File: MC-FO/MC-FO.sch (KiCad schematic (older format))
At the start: 0 parts

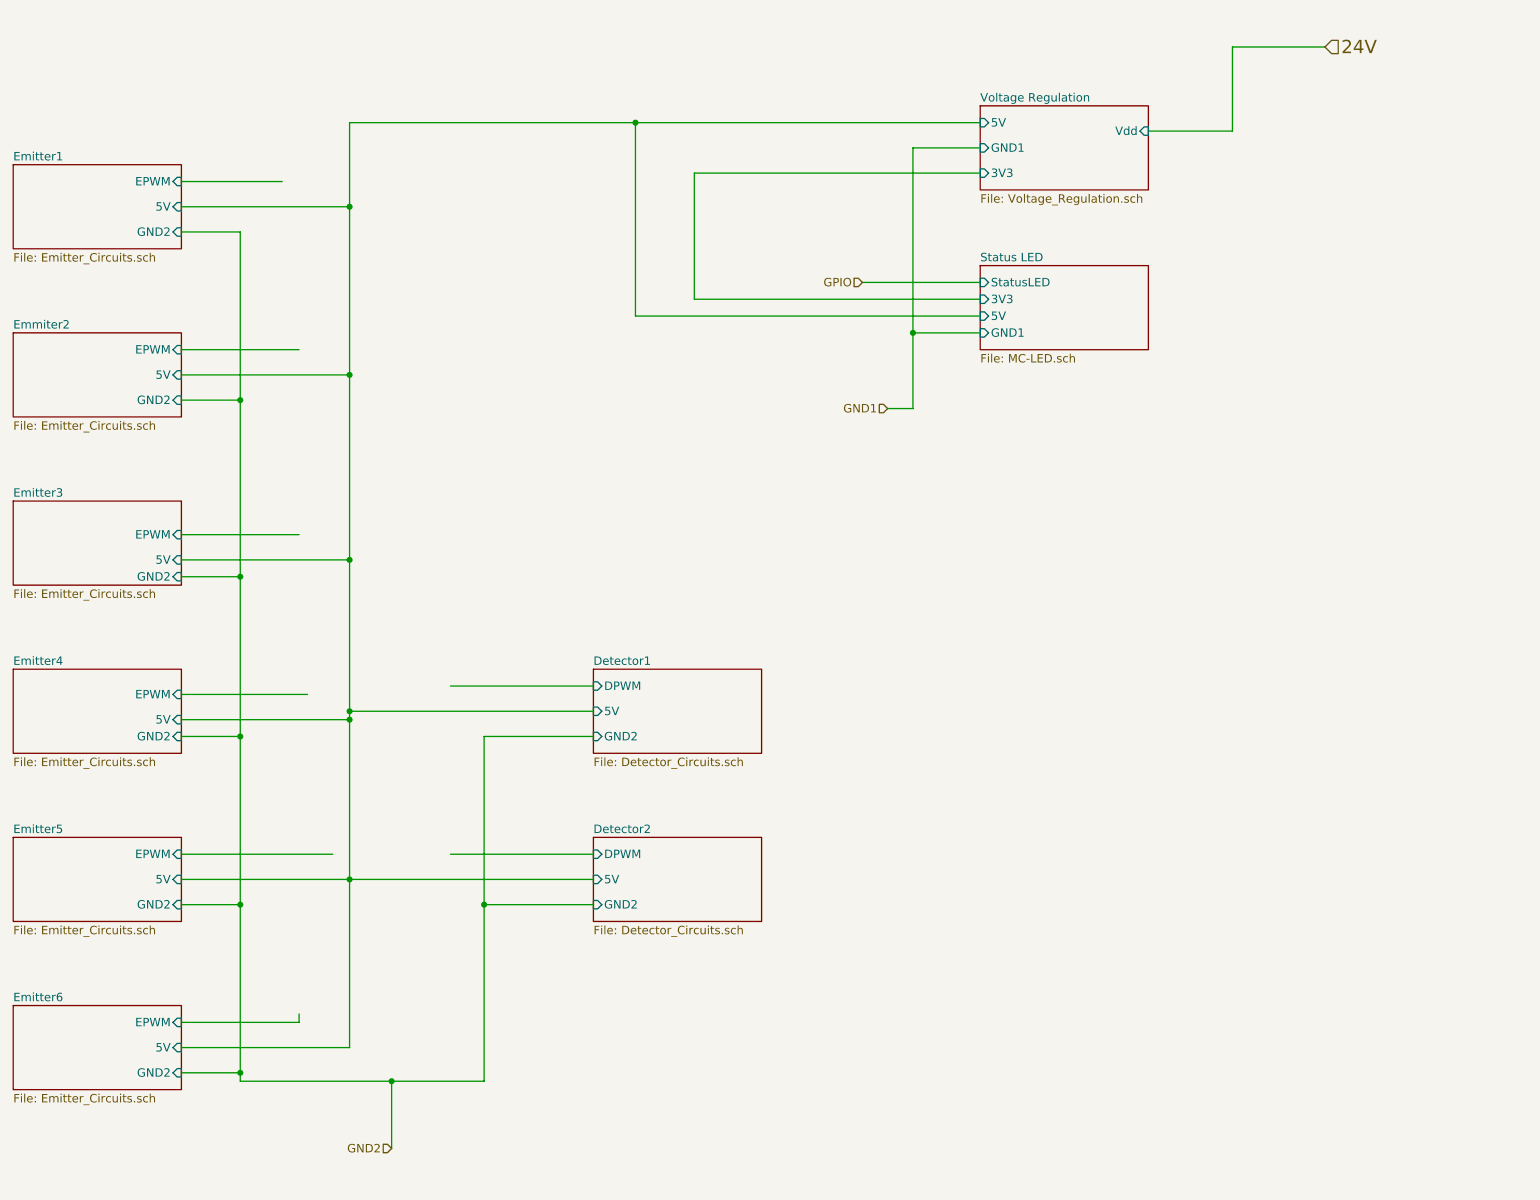
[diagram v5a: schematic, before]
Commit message: a few more FO tweaks 10-26
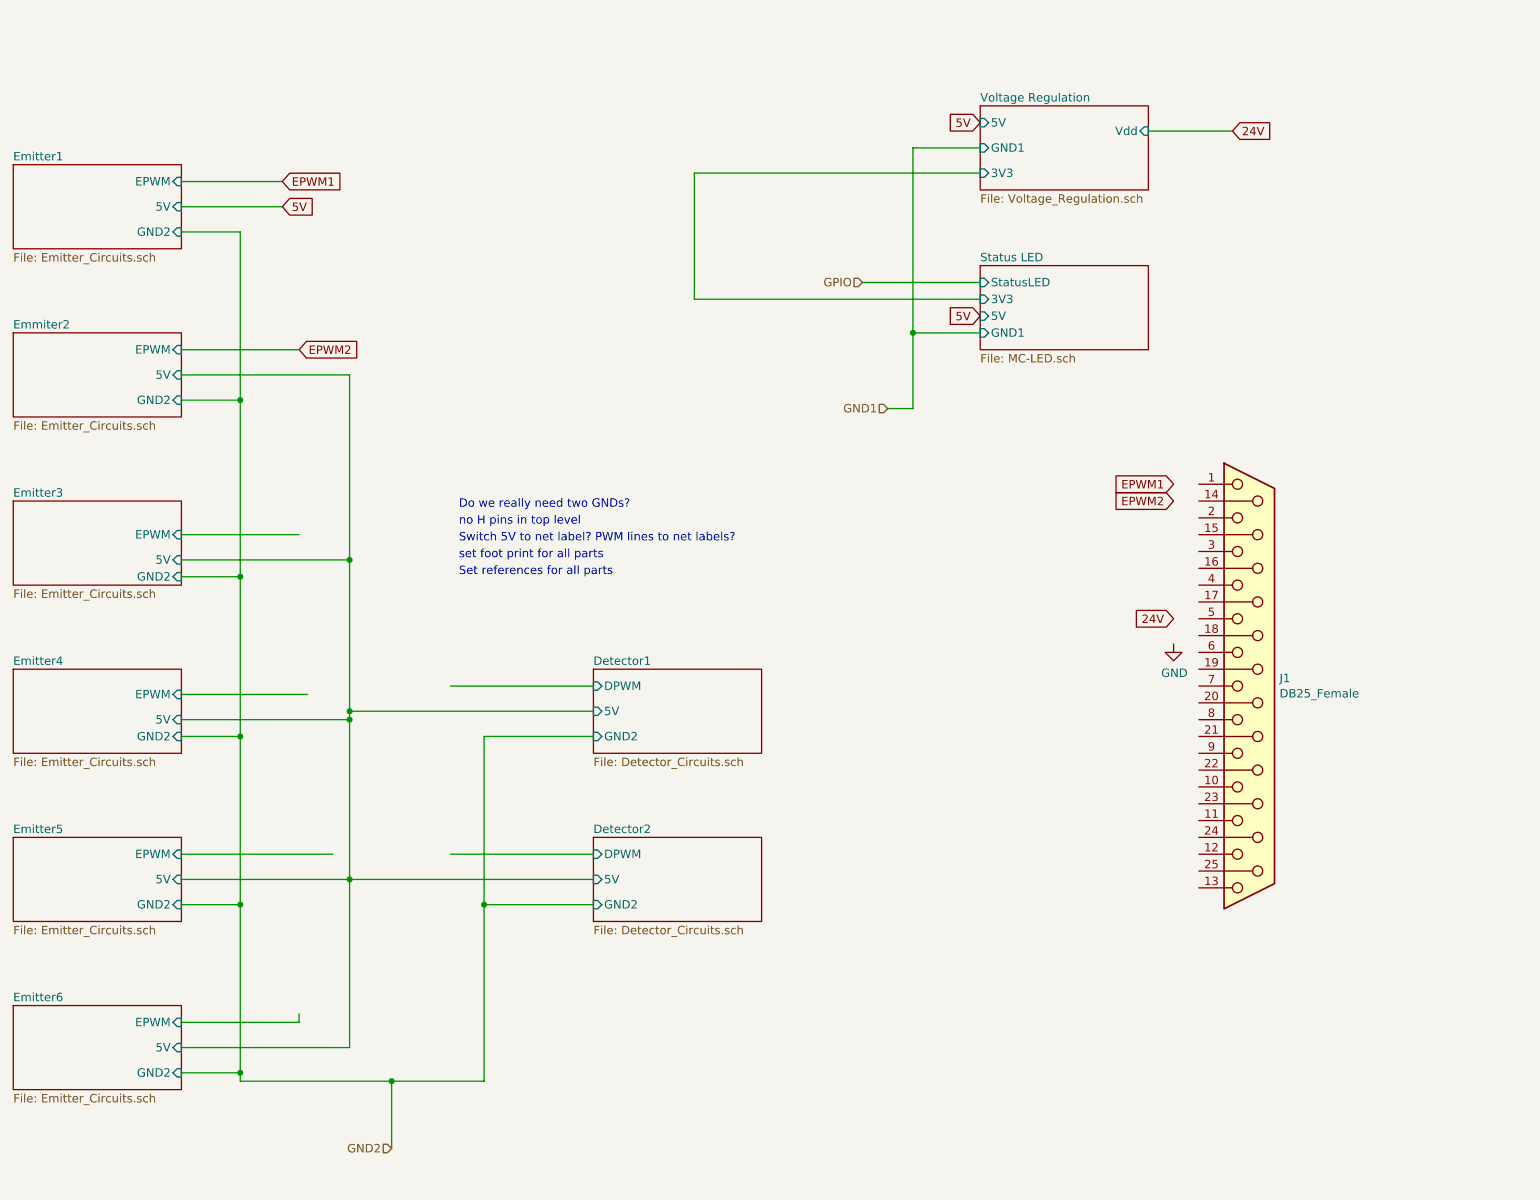
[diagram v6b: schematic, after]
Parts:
- added J1: DB25_Female, symbol Connector:DB25_Female
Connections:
- net labels added: 5V, EPWM1, EPWM2, GND
- wire segments 59 -> 51
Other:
- note added: "Do we really need two GNDs?"
- note added: "Set references for all parts\n"
- note added: "Switch 5V to net label? PWM lines to net labels?"
- note added: "no H pins in top level\n"
- note added: "set foot print for all parts\n"
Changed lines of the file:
@@
 F4 "GND2" I R 2500 3950 50
 $EndSheet
-Text HLabel 9300 800  2    79   Input ~ 0
-24V
 Wire Wire Line
 	2500 2600 3200 2600
@@
 Wire Wire Line
 	2500 1600 3100 1600
-Wire Wire Line
-	3500 1750 2500 1750
 Wire Wire Line
 	3500 6750 2500 6750
@@
 Wire Wire Line
 	2500 2750 3500 2750
-Connection ~ 3500 2750
 Wire Wire Line
 	3500 4800 3500 4750
@@
 $EndSheet
 Wire Wire Line
-	9300 800  8750 800
-Wire Wire Line
-	8750 800  8750 1300
-Wire Wire Line
-	8250 1300 8750 1300
-Connection ~ 3500 1750
-Wire Wire Line
-	3500 1750 3500 2750
-Wire Wire Line
-	7250 1250 5200 1250
-Wire Wire Line
-	3500 1250 3500 1750
-Wire Wire Line
 	7250 1550 5550 1550
 Wire Wire Line
@@
 Wire Wire Line
 	6850 2500 6850 2950
-Wire Wire Line
-	5200 1250 5200 2400
-Wire Wire Line
-	5200 2400 7250 2400
-Connection ~ 5200 1250
-Wire Wire Line
-	5200 1250 3500 1250
 Text HLabel 6700 2950 0    50   Input ~ 0
 GND1
@@
 Text HLabel 3750 7350 0    50   Input ~ 0
 GND2
+Text Notes 4150 3550 0    50   ~ 0
+Do we really need two GNDs?
+Text Notes 4150 3650 0    50   ~ 0
+no H pins in top level\n
+Text GLabel 3100 1600 2    50   Input ~ 0
+EPWM1
+Text GLabel 3200 2600 2    50   Input ~ 0
+EPWM2
+Text GLabel 3100 1750 2    50   Input ~ 0
+5V
+Wire Wire Line
+	3100 1750 2500 1750
+Text Notes 4150 3750 0    50   ~ 0
+Switch 5V to net label? PWM lines to net labels?
+Text GLabel 7250 1250 0    50   Input ~ 0
+5V
+Text GLabel 7250 2400 0    50   Input ~ 0
+5V
+Text GLabel 8400 3400 0    50   Input ~ 0
+EPWM1
+Text GLabel 8400 3500 0    50   Input ~ 0
+EPWM2
+Text GLabel 8750 1300 2    50   Input ~ 0
+24V
+Wire Wire Line
+	8750 1300 8250 1300
+Text GLabel 8400 4200 0    50   Input ~ 0
+24V
+$Comp
+L power:GND #PWR?
+U 1 1 6179D3DC
+P 8400 4350
+F 0 "#PWR?" H 8400 4100 50  0001 C CNN
+F 1 "GND" H 8405 4177 50  0000 C CNN
+F 2 "" H 8400 4350 50  0001 C CNN
+F 3 "" H 8400 4350 50  0001 C CNN
+	1    8400 4350
+	1    0    0    -1
+$EndComp
+$Comp
+L Connector:DB25_Female J1
+U 1 1 6179E2FC
+P 8850 4600
+F 0 "J1" H 9030 4646 50  0000 L CNN
+F 1 "DB25_Female" H 9030 4555 50  0000 L CNN
+F 2 "" H 8850 4600 50  0001 C CNN
+F 3 " ~" H 8850 4600 50  0001 C CNN
+	1    8850 4600
+	1    0    0    -1
+$EndComp
+Text Notes 4150 3850 0    50   ~ 0
+set foot print for all parts\n
+Text Notes 4150 3950 0    50   ~ 0
+Set references for all parts\n
 $EndSCHEMATC

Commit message: added footprints and reference
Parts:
- J1: footprint (none) -> Connector_Dsub:DSUB-25_Female_Horizontal_P2.77x2.54mm_EdgePinOffset9.40mm
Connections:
- net labels added: DPWM1, DPWM2, EPWM3, EPWM4, EPWM5, EPWM6
- net labels removed: 5V, GND
- wire segments 51 -> 68
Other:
- note removed: "Switch 5V to net label? PWM lines to net labels?"
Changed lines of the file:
@@
 $EndSheet
 Wire Wire Line
-	2500 2600 3200 2600
-Wire Wire Line
-	2500 3700 3200 3700
-Wire Wire Line
-	2500 4650 3250 4650
-Wire Wire Line
-	2500 5600 3400 5600
+	2500 3700 3150 3700
+Wire Wire Line
+	2500 4650 3150 4650
+Wire Wire Line
+	2500 5600 3150 5600
 Wire Wire Line
 	2500 1600 3100 1600
@@
 	2850 2900 2850 3950
 Wire Wire Line
-	3200 6600 3200 6550
-Wire Wire Line
-	2500 6600 3200 6600
+	2500 6600 3150 6600
 Wire Wire Line
 	3500 4800 3500 5750
@@
 	4300 6950 3750 6950
 Connection ~ 3750 6950
-Text HLabel 6550 2200 0    50   Input ~ 0
-GPIO
 Wire Wire Line
 	6850 2500 6850 2950
-Text HLabel 6700 2950 0    50   Input ~ 0
-GND1
 Wire Wire Line
 	6850 2950 6700 2950
-Text HLabel 3750 7350 0    50   Input ~ 0
-GND2
 Text Notes 4150 3550 0    50   ~ 0
 Do we really need two GNDs?
@@
 Text GLabel 3100 1600 2    50   Input ~ 0
 EPWM1
-Text GLabel 3200 2600 2    50   Input ~ 0
+Text GLabel 3100 2600 2    50   Input ~ 0
 EPWM2
-Text GLabel 3100 1750 2    50   Input ~ 0
-5V
-Wire Wire Line
-	3100 1750 2500 1750
-Text Notes 4150 3750 0    50   ~ 0
-Switch 5V to net label? PWM lines to net labels?
-Text GLabel 7250 1250 0    50   Input ~ 0
-5V
-Text GLabel 7250 2400 0    50   Input ~ 0
-5V
-Text GLabel 8400 3400 0    50   Input ~ 0
+Text GLabel 8250 3400 0    50   Input ~ 0
 EPWM1
-Text GLabel 8400 3500 0    50   Input ~ 0
+Text GLabel 8250 3600 0    50   Input ~ 0
 EPWM2
 Text GLabel 8750 1300 2    50   Input ~ 0
@@
 Wire Wire Line
 	8750 1300 8250 1300
-Text GLabel 8400 4200 0    50   Input ~ 0
+Text GLabel 7900 3500 0    50   Input ~ 0
 24V
-$Comp
-L power:GND #PWR?
-U 1 1 6179D3DC
-P 8400 4350
-F 0 "#PWR?" H 8400 4100 50  0001 C CNN
-F 1 "GND" H 8405 4177 50  0000 C CNN
-F 2 "" H 8400 4350 50  0001 C CNN
-F 3 "" H 8400 4350 50  0001 C CNN
-	1    8400 4350
-	1    0    0    -1
-$EndComp
 $Comp
 L Connector:DB25_Female J1
@@
 F 0 "J1" H 9030 4646 50  0000 L CNN
 F 1 "DB25_Female" H 9030 4555 50  0000 L CNN
-F 2 "" H 8850 4600 50  0001 C CNN
+F 2 "Connector_Dsub:DSUB-25_Female_Horizontal_P2.77x2.54mm_EdgePinOffset9.40mm" H 8850 4600 50  0001 C CNN
 F 3 " ~" H 8850 4600 50  0001 C CNN
 	1    8850 4600
@@
 Text Notes 4150 3950 0    50   ~ 0
 Set references for all parts\n
+Text GLabel 8250 3800 0    50   Input ~ 0
+EPWM3
+Text GLabel 8250 4000 0    50   Input ~ 0
+EPWM4
+Text GLabel 8250 4200 0    50   Input ~ 0
+EPWM5
+Text GLabel 8250 4400 0    50   Input ~ 0
+EPWM6
+Text GLabel 8250 4800 0    50   Input ~ 0
+DPWM1
+Text GLabel 8250 5000 0    50   Input ~ 0
+DPWM2
+Text GLabel 3150 3700 2    50   Input ~ 0
+EPWM3
+Text GLabel 3150 4650 2    50   Input ~ 0
+EPWM4
+Text GLabel 3150 5600 2    50   Input ~ 0
+EPWM5
+Text GLabel 3150 6600 2    50   Input ~ 0
+EPWM6
+Text GLabel 8250 5200 0    50   Input ~ 0
+GPIO
+Wire Wire Line
+	8550 3400 8250 3400
+Wire Wire Line
+	8550 3600 8250 3600
+Wire Wire Line
+	8550 3500 7900 3500
+Wire Wire Line
+	8550 3800 8250 3800
+Wire Wire Line
+	8550 4000 8250 4000
+Wire Wire Line
+	8550 4200 8250 4200
+Wire Wire Line
+	8550 4400 8250 4400
+Wire Wire Line
+	8550 4800 8250 4800
+Wire Wire Line
+	8550 5000 8250 5000
+Wire Wire Line
+	8550 5200 8250 5200
+Wire Wire Line
+	8100 5700 8550 5700
+Wire Wire Line
+	8100 5700 8100 5850
+Text GLabel 4100 4600 0    50   Input ~ 0
+DPWM1
+Text GLabel 4100 5600 0    50   Input ~ 0
+DPWM2
+Wire Wire Line
+	7250 1250 5200 1250
+Wire Wire Line
+	3500 1250 3500 1750
+Wire Wire Line
+	2500 1750 3500 1750
+Wire Wire Line
+	3500 1750 3500 2750
+Connection ~ 3500 1750
+Connection ~ 3500 2750
+Wire Wire Line
+	3100 2600 2500 2600
+$Comp
+L power:GND1 #PWR02
+U 1 1 617AD6F4
+P 6700 2950
+F 0 "#PWR02" H 6700 2700 50  0001 C CNN
+F 1 "GND1" H 6705 2777 50  0000 C CNN
+F 2 "" H 6700 2950 50  0001 C CNN
+F 3 "" H 6700 2950 50  0001 C CNN
+	1    6700 2950
+	1    0    0    -1
+$EndComp
+$Comp
+L power:GND2 #PWR01
+U 1 1 617AF034
+P 3750 7350
+F 0 "#PWR01" H 3750 7100 50  0001 C CNN
+F 1 "GND2" H 3755 7177 50  0000 C CNN
+F 2 "" H 3750 7350 50  0001 C CNN
+F 3 "" H 3750 7350 50  0001 C CNN
+	1    3750 7350
+	1    0    0    -1
+$EndComp
+$Comp
+L power:GND1 #PWR03
+U 1 1 617AF950
+P 8100 5850
+F 0 "#PWR03" H 8100 5600 50  0001 C CNN
+F 1 "GND1" H 8105 5677 50  0000 C CNN
+F 2 "" H 8100 5850 50  0001 C CNN
+F 3 "" H 8100 5850 50  0001 C CNN
+	1    8100 5850
+	1    0    0    -1
+$EndComp
+Text GLabel 6550 2200 0    50   Input ~ 0
+GPIO
+Wire Wire Line
+	5200 1250 5200 2400
+Wire Wire Line
+	5200 2400 7250 2400
+Connection ~ 5200 1250
+Wire Wire Line
+	5200 1250 3500 1250
 $EndSCHEMATC
